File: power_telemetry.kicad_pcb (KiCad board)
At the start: 2 copper layers, 86.5 x 50 mm, 49 parts, among them J1 Screw_Terminal_1x02, J10 CONN_01X04, J11 CONN_01X04, J12 GS2, J2 CONN_01X02, J3 CONN_01X03, J4 CONN_01X02, J5 CONN_01X02, J6 CONN_01X03, J7 CONN_01X02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

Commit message: now using 4 pad shunt resistor
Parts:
- R1: footprint lib_fp:R_2512_Kelvin_HandSoldering -> lib_fp:R_2512_Kelvin2_HandSoldering
- moved R2 2.24 mm to (98.0, 90.0), turned to 0 degrees
- moved R3 2.10 mm to (98.0, 79.7), turned to 0 degrees
- moved C3 1.45 mm to (100.7, 84.7)
- moved C4 1.45 mm to (105.8, 79.5)
- moved R5 1.45 mm to (107.5, 88.6)
- moved U1 1.45 mm to (106.5, 83.7)
- moved C5 1.45 mm to (105.8, 77.1)
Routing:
- net Net-(J1-Pad1): track 13.5 -> 11.2 mm
- net /SCL: track 91.4 -> 89.2 mm
- net VCC: track 157.3 -> 155.5 mm
- net /SDA: track 73.0 -> 72.0 mm
- net Net-(C3-Pad1): track 6.84 -> 7.45 mm

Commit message: changed sense resistor to 4527
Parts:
- R1: footprint lib_fp:R_2512_Kelvin2_HandSoldering -> lib_fp:R_4527_HandSoldering
- moved REF** 12.5 mm to (82.0, 82.5)
- moved J1 7.14 mm to (83.4, 95.6)
- moved C3 4.64 mm to (105.4, 84.7)
- moved C4 4.64 mm to (110.5, 79.4)
- moved C5 4.64 mm to (110.5, 77.0)
- moved R2 4.64 mm to (102.7, 89.9)
- moved R3 4.64 mm to (102.7, 79.6)
- moved R5 4.64 mm to (112.1, 88.5)
- moved U1 4.64 mm to (111.2, 83.6)
- moved R1 2.64 mm to (94.5, 84.7)
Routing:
- net Net-(J1-Pad1): track 11.2 -> 21.3 mm
- net /SCL: track 89.2 -> 80.0 mm
- net /SDA: track 72.0 -> 67.4 mm
- net +12V: track 67.7 -> 63.1 mm
- net VCC: track 155.5 -> 151.8 mm
- net Net-(C3-Pad2): track 7.29 -> 8.27 mm

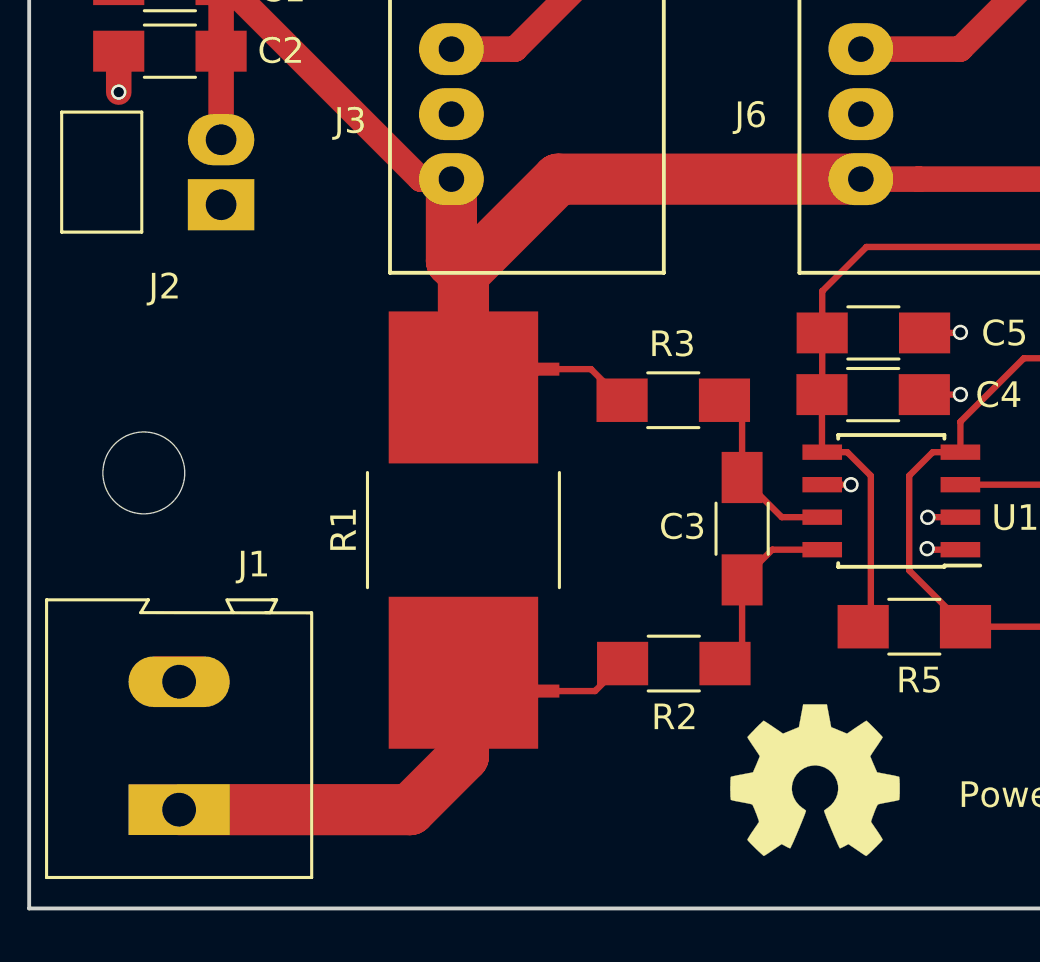
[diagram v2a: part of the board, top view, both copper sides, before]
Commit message: fully switched to another sense resistor
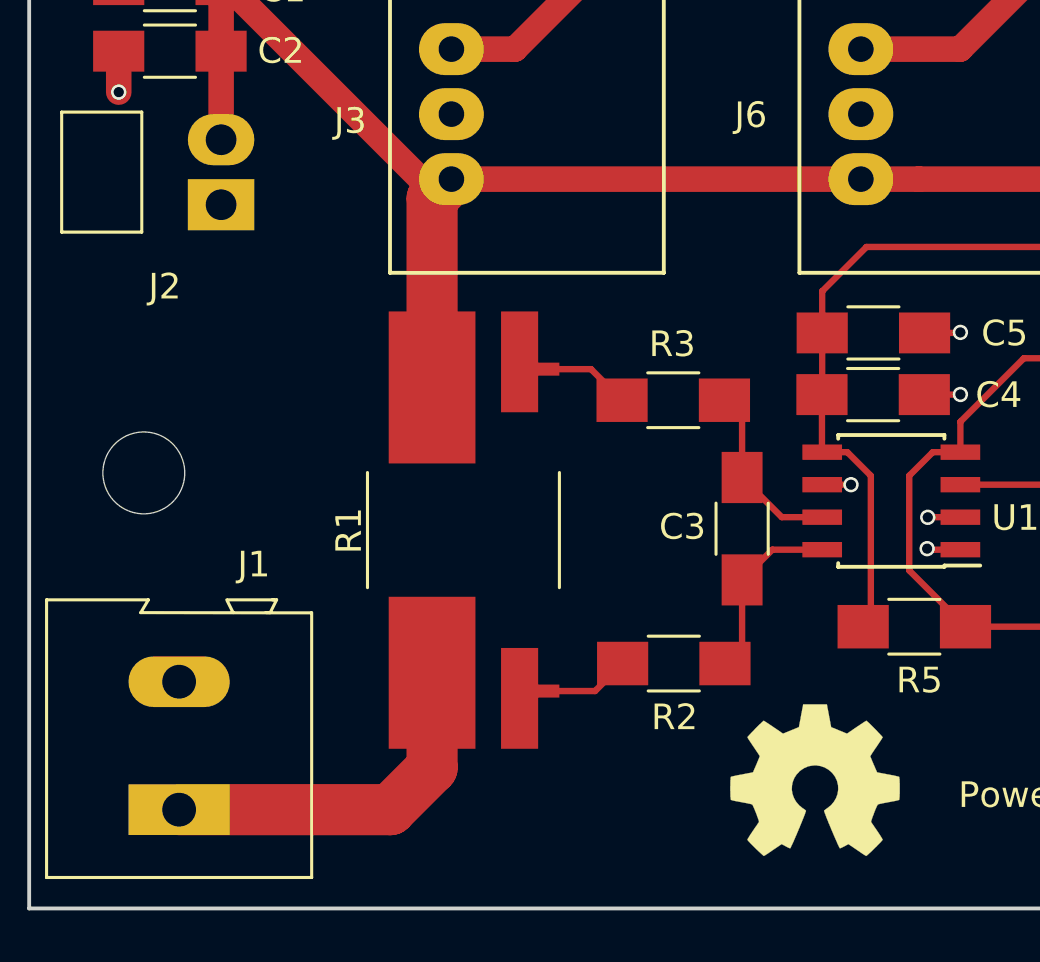
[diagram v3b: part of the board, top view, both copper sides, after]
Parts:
- R1: value 6.5 mOhms -> 100 mOhms; footprint lib_fp:R_4527_HandSoldering -> lib_fp:R_4527_Kelvin2_HandSoldering
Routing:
- net Net-(J1-Pad1): track 21.3 -> 17.8 mm
- net +12V: track 63.1 -> 62.2 mm
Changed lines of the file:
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@@
 (kicad_pcb (version 4) (host pcbnew 4.0.7)
   (general
-    (links 91)
-    (no_connects 2)
-    (area 71.944999 43.944999 168.655001 100.892382)
+    (links 93)
+    (no_connects 4)
+    (area 77.424999 49.424999 164.075001 99.575001)
     (thickness 1.6)
     (drawings 5)
-    (tracks 242)
+    (tracks 239)
     (zones 0)
     (modules 49)
@@
   )
   (setup
-    (last_trace_width 2)
+    (last_trace_width 1)
     (user_trace_width 0.51)
     (user_trace_width 1)
@@
     (pad 1 np_thru_hole circle (at 0 0) (size 3.2 3.2) (drill 3.2) (layers *.Cu *.Mask))
   )
-  (module lib_fp:R_4527_HandSoldering (layer F.Cu)
+  (module lib_fp:R_4527_Kelvin2_HandSoldering (layer F.Cu)
     (at 94.47 84.715 90)
     (descr "Resistor SMD 4527, hand soldering, Vishay (see WSR5)")
     (tags "resistor 4527")
     (attr smd)
-    (fp_text reference R1 (at 0.005 -4.67 90) (layer F.SilkS)
-      (effects (font (size 1 1) (thickness 0.15)))
-    )
-    (fp_text value "6.5 mOhms" (at 0 4.5847 90) (layer F.Fab)
+    (fp_text reference R1 (at -0.02032 -4.46998 90) (layer F.SilkS)
+      (effects (font (size 1 1) (thickness 0.15)))
+    )
+    (fp_text value "100 mOhms" (at 0 4.5847 90) (layer F.Fab)
       (effects (font (size 1 1) (thickness 0.15)))
     )
@@
     (fp_line (start 6.795 3.74) (end 6.795 -3.74) (layer F.CrtYd) (width 0.05))
     (fp_line (start 6.795 3.74) (end -6.795 3.74) (layer F.CrtYd) (width 0.05))
+    (pad 2 smd rect (at 6.575 2.195 90) (size 3.94 1.45) (layers F.Cu F.Paste F.Mask)
+      (net 2 +12V))
+    (pad 2 smd rect (at 5.575 -1.225 90) (size 5.94 3.39) (layers F.Cu F.Paste F.Mask)
+      (net 2 +12V))
+    (pad 1 smd rect (at -6.575 2.195 90) (size 3.94 1.45) (layers F.Cu F.Paste F.Mask)
+      (net 6 "Net-(J1-Pad1)"))
     (pad 2 smd rect (at 6.29 3.25 90) (size 0.51 1) (layers F.Cu F.Paste F.Mask)
       (net 2 +12V))
     (pad 1 smd rect (at -6.29 3.25 90) (size 0.51 1) (layers F.Cu F.Paste F.Mask)
       (net 6 "Net-(J1-Pad1)"))
-    (pad 1 smd rect (at -5.575 0 90) (size 5.94 5.84) (layers F.Cu F.Paste F.Mask)
+    (pad 1 smd rect (at -5.575 -1.225 90) (size 5.94 3.39) (layers F.Cu F.Paste F.Mask)
       (net 6 "Net-(J1-Pad1)"))
-    (pad 2 smd rect (at 5.575 0 90) (size 5.94 5.84) (layers F.Cu F.Paste F.Mask)
-      (net 2 +12V))
     (model ${KISYS3DMOD}/Resistors_SMD.3dshapes/R_2816.wrl
       (at (xyz 0 0 0))
@@
   (segment (start 98.3 53) (end 96.8 53) (width 1) (layer F.Cu) (net 1))
   (via (at 96.8 53) (size 0.6) (drill 0.4) (layers F.Cu B.Cu) (net 1))
+  (segment (start 94 71) (end 110 71) (width 1) (layer F.Cu) (net 2) (status C00000))
+  (segment (start 93.245 79.14) (end 93.245 71.755) (width 2) (layer F.Cu) (net 2) (status C00000))
+  (segment (start 93.245 71.755) (end 94 71) (width 2) (layer F.Cu) (net 2) (status C00000))
   (segment (start 97.72 78.425) (end 99.455 78.425) (width 0.25) (layer F.Cu) (net 2))
   (segment (start 99.455 78.425) (end 100.67 79.64) (width 0.25) (layer F.Cu) (net 2))
-  (segment (start 94.47 79.14) (end 94.47 74.7) (width 2) (layer F.Cu) (net 2))
-  (segment (start 94 74.2) (end 94 71) (width 2) (layer F.Cu) (net 2))
-  (segment (start 94.485 74.685) (end 98.17 71) (width 2) (layer F.Cu) (net 2))
-  (segment (start 98.17 71) (end 110 71) (width 2) (layer F.Cu) (net 2))
-  (segment (start 94.485 74.685) (end 94 74.2) (width 2) (layer F.Cu) (net 2))
   (segment (start 85 66) (end 85 69.46) (width 1) (layer F.Cu) (net 2))
   (segment (start 85 63.4) (end 85 66) (width 1) (layer F.Cu) (net 2))
@@
   (segment (start 132.3 57) (end 128.84 57) (width 1) (layer F.Cu) (net 5))
   (segment (start 134.9 57) (end 132.3 57) (width 1) (layer F.Cu) (net 5))
-  (segment (start 83.36 95.64) (end 92.38 95.64) (width 2) (layer F.Cu) (net 6))
-  (segment (start 94.47 93.55) (end 94.47 90.29) (width 2) (layer F.Cu) (net 6))
-  (segment (start 92.38 95.64) (end 94.47 93.55) (width 2) (layer F.Cu) (net 6))
+  (segment (start 83.36 95.64) (end 91.61 95.64) (width 2) (layer F.Cu) (net 6) (status 400000))
+  (segment (start 93.245 94.005) (end 93.245 90.29) (width 2) (layer F.Cu) (net 6) (status 800000))
+  (segment (start 91.61 95.64) (end 93.245 94.005) (width 2) (layer F.Cu) (net 6))
   (segment (start 97.72 91.005) (end 99.615 91.005) (width 0.25) (layer F.Cu) (net 6))
   (segment (start 99.615 91.005) (end 100.69 89.93) (width 0.25) (layer F.Cu) (net 6))
-  (segment (start 92.68 88.5) (end 94.47 90.29) (width 2) (layer F.Cu) (net 6))
   (segment (start 101.23 89.43) (end 101.38 89.43) (width 0.25) (layer F.Cu) (net 6))
   (segment (start 113.89 82.94) (end 117.53 82.94) (width 0.25) (layer F.Cu) (net 7))
